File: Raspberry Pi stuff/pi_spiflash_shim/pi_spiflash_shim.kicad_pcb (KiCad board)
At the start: 2 copper layers, 19 x 12.7 mm, 3 parts, among them J1 Conn_02x05_Odd_Even, U1 W25Q32JVSS

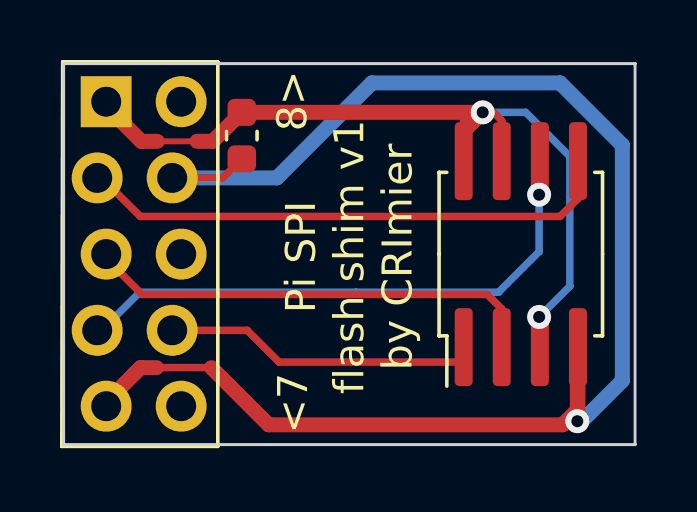
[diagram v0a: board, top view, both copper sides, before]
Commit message: pi_spiflash_shim: moving text a bit, removing a prl file from git
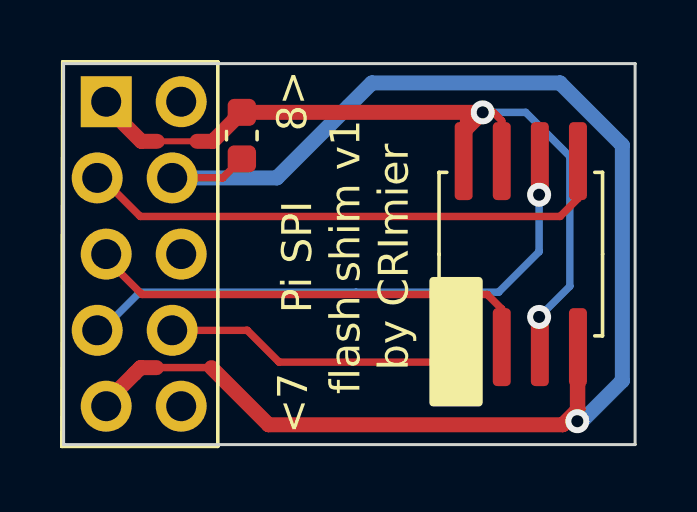
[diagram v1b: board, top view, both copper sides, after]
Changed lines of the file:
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@@
     (effects (font (size 1 1) (thickness 0.15)))
   )
-  (gr_text "Pi SPI\nflash shim v1\nby CRImier" (at 161.925 81.375 90) (layer "F.SilkS")
+  (gr_text "Pi SPI\nflash shim v1\nby CRImier" (at 161.798 81.375 90) (layer "F.SilkS")
     (effects (font (size 1 1) (thickness 0.15)))
   )
@@
   (segment (start 158.5214 83.82) (end 159.5814 84.88) (width 0.25) (layer "F.Cu") (net 8))
   (segment (start 159.5814 84.88) (end 165.735 84.88) (width 0.25) (layer "F.Cu") (net 8))
+  (zone (net 0) (net_name "") (layer "F.SilkS") (hatch edge 0.508)
+    (connect_pads (clearance 0.508))
+    (min_thickness 0.254) (filled_areas_thickness no)
+    (fill yes (thermal_gap 0.508) (thermal_bridge_width 0.508))
+    (polygon
+      (pts
+        (xy 166.37 86.36)
+        (xy 164.592 86.36)
+        (xy 164.592 82.042)
+        (xy 166.37 82.042)
+      )
+    )
+  )
 )
